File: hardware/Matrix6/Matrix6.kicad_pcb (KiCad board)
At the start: 4 copper layers, 40.6 x 61 mm, 48 parts, among them J1 USB4105-GF-A-120, J2 microSD (rear), J3 LiPo 1S / PH2, Q1 AO3401A, SW1 RESET, SW2 BOOT, U1 ESP32-S3-WROOM-1-N8R8, U2 TPS63001 (3.3V), U3 USBLC6-2SC6, U4 MCP73831 / 100mA

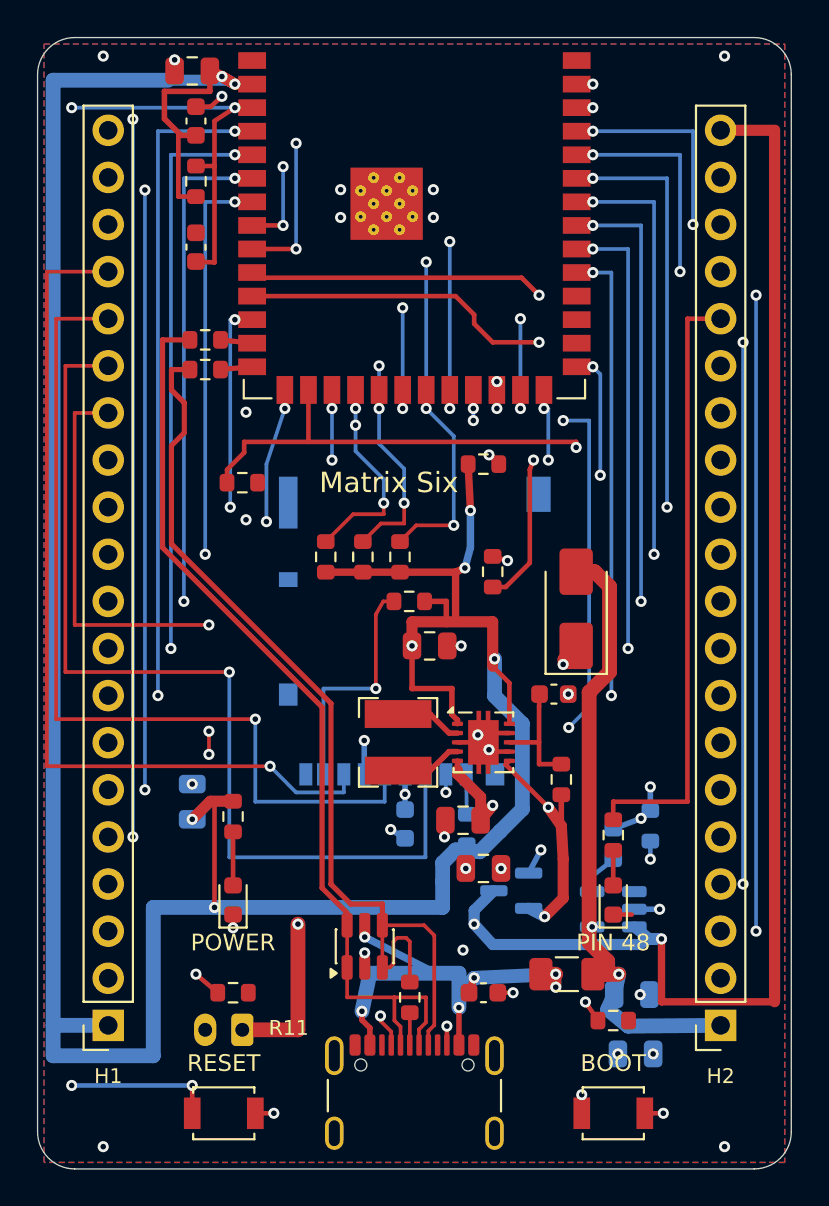
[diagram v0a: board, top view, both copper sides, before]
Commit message: Redesign Matrix Six v0.8 for two copper layers
Manually reroute signal and power nets, match the top-only USB pair with coplanar ground, and enlarge thermal drills to 0.3 mm. Preserve Matrix5 shield mapping, R2 outline, rear SD access and LiPo functions. Enlarge the front Matrix Six title and place its design credit beneath it. Include DRC/ERC, geometry and electrical screening, 30-degree renders, manufacturing files and a JLCPCB cost comparison.
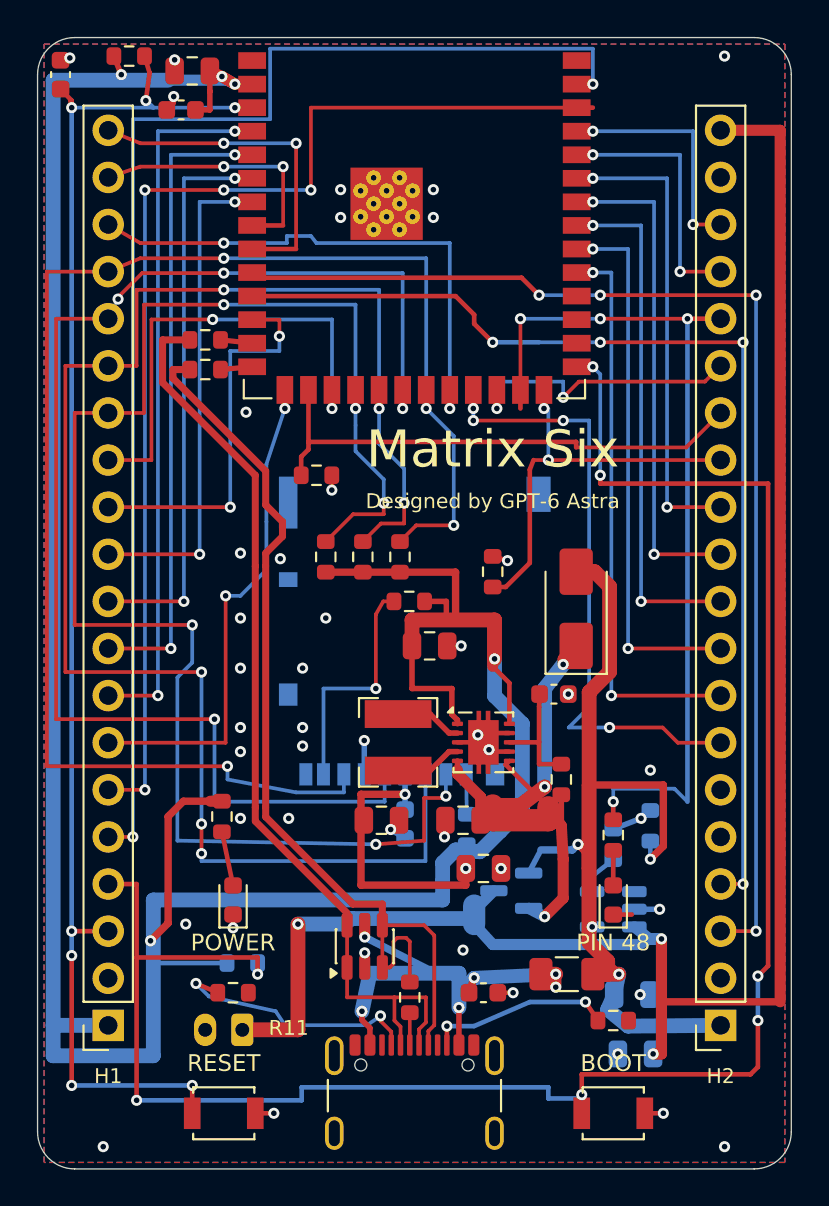
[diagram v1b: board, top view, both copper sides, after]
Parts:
- C11: moved to F.Cu
- R6: moved to B.Cu
- moved R6 29.9 mm to (108.5, 149.9)
- moved C5 11.8 mm to (98.7, 102.0)
- moved C11 10.2 mm to (116.0, 142.2), turned to 0 degrees
- moved R5 7.65 mm to (102.4, 101.0), turned to 0 degrees
- moved R8 4.02 mm to (112.5, 123.6)
- moved C4 1.00 mm to (105.2, 103.9), turned to 180 degrees
- moved R9 0.60 mm to (107.4, 142.0)
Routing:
- net /IO10: track 66.8 -> 85.4 mm, vias 7 -> 6
- net /VBUS_FUSED: track 53.7 -> 63.3 mm
- net /IO9: track 15.8 -> 25.4 mm
- net /IO11: track 80.0 -> 88.6 mm, vias 4 -> 6
- net /+3V3: track 203.5 -> 195.9 mm, vias 10 -> 7
- net /EN: track 83.4 -> 77.1 mm, vias 4 -> 7
- net /IO46: track 32.1 -> 28.1 mm, vias 1 -> 0
- net /IO1: track 67.6 -> 71.4 mm, vias 3 -> 2
- net /IO12: track 70.4 -> 73.5 mm, vias 3 -> 4
- net /IO8: track 17.9 -> 20.8 mm
- net /IO0: track 105.3 -> 107.0 mm, vias 4 -> 7
- net /IO47: track 14.9 -> 16.1 mm
- net /IO48: track 49.4 -> 50.4 mm, vias 2 -> 4
- net /IO3: track 27.7 -> 26.9 mm
- net /CC1: track 14.4 -> 13.7 mm
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- removed copper zone on In1.Cu, net /GND
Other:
- copper layers 4 -> 2
- board text added: "Designed by GPT-6 Astra"
- board text removed: "Designed By GPT-6 Astra"

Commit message: Center front branding and move R8 beside the module
Align both silkscreen lines to the board centre and move the IO46 pull-down to clear the title area. Reroute its branch explicitly, refill ground and regenerate manufacturing data, CPL and 3D previews. DRC, ERC and unrouted counts remain zero; USB and all other signal routing are preserved.
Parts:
- moved R8 17.1 mm to (129.3, 120.3), turned to 90 degrees
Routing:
- net /IO46: track 28.1 -> 27.1 mm
- net /GND: track 22.3 -> 21.5 mm, vias 45 -> 44
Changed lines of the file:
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@@
 	(footprint "Resistor_SMD:R_0603_1608Metric"
 		(layer "F.Cu")
-		(at 112.5 123.6)
+		(at 129.3 120.3 90)
 		(descr "Resistor SMD 0603 (1608 Metric), square (rectangular) end terminal, IPC-7351 nominal, (Body size source: IPC-SM-782 page 72, https://www.pcb-3d.com/wordpress/wp-content/uploads/ipc-sm-782a_amendment_1_and_2.pdf)")
 		(tags "resistor")
 		(property "Reference" "R8"
-			(at 0 -1.43 0)
+			(at 0 -1.43 90)
 			(layer "F.SilkS")
 			(hide yes)
@@
 		)
 		(property "Value" "10k 1%"
-			(at 0 1.43 0)
+			(at 0 1.43 90)
 			(layer "F.Fab")
 			(hide yes)
@@
 		)
 		(property "Datasheet" ""
-			(at 0 0 0)
+			(at 0 0 90)
 			(layer "F.Fab")
 			(hide yes)
@@
 		)
 		(property "Description" ""
-			(at 0 0 0)
+			(at 0 0 90)
 			(layer "F.Fab")
 			(hide yes)
@@
 		)
 		(property "KiLib_Generator" "SMD_2terminal_chip_molded"
-			(at 0 0 0)
+			(at 0 0 90)
 			(layer "F.SilkS")
 			(hide yes)
@@
 		)
 		(fp_text user "${REFERENCE}"
-			(at 0 0 0)
+			(at 0 0 90)
 			(layer "F.Fab")
 			(effects
@@
 		)
 		(pad "1" smd roundrect
-			(at -0.825 0)
+			(at -0.825 0 90)
 			(size 0.8 0.95)
 			(layers "F.Cu" "F.Mask" "F.Paste")
@@
 		)
 		(pad "2" smd roundrect
-			(at 0.825 0)
+			(at 0.825 0 90)
 			(size 0.8 0.95)
 			(layers "F.Cu" "F.Mask" "F.Paste")
@@
 	)
 	(gr_text "Designed by GPT-6 Astra"
-		(at 122 125 0)
+		(at 117.78 125 0)
 		(layer "F.SilkS")
 		(effects
@@
 	)
 	(gr_text "Matrix Six"
-		(at 122 122.2 0)
+		(at 117.78 122.2 0)
 		(layer "F.SilkS")
 		(effects
@@
 	)
 	(segment
-		(start 113.325 123.6)
-		(end 113.325 124.4)
-		(width 0.25)
-		(layer "F.Cu")
-		(net "/GND")
-	)
-	(segment
 		(start 108 147.2875)
 		(end 108 148)
@@
 	)
 	(via
-		(at 113.325 124.4)
-		(size 0.6)
-		(drill 0.3)
-		(layers "F.Cu" "B.Cu")
-		(net "/GND")
-	)
-	(via
 		(at 99.2 101.1)
 		(size 0.6)
@@
 	)
 	(segment
-		(start 111.675 122.6)
-		(end 112.065 122.21)
-		(width 0.25)
-		(layer "F.Cu")
-		(net "/IO46")
-	)
-	(segment
-		(start 112.065 122.21)
-		(end 112.065 121.8)
-		(width 0.25)
-		(layer "F.Cu")
-		(net "/IO46")
-	)
-	(segment
 		(start 132.43 122.1)
 		(end 134.29 120.24)
@@
 	)
 	(segment
-		(start 111.675 123.6)
-		(end 111.675 122.6)
+		(start 112.065 119)
+		(end 112.065 121.8)
 		(width 0.25)
 		(layer "F.Cu")
@@
 	)
 	(segment
-		(start 112.065 119)
-		(end 112.065 121.8)
+		(start 129.3 122.1)
+		(end 129.3 121.125)
 		(width 0.25)
 		(layer "F.Cu")
